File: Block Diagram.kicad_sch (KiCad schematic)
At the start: 0 parts

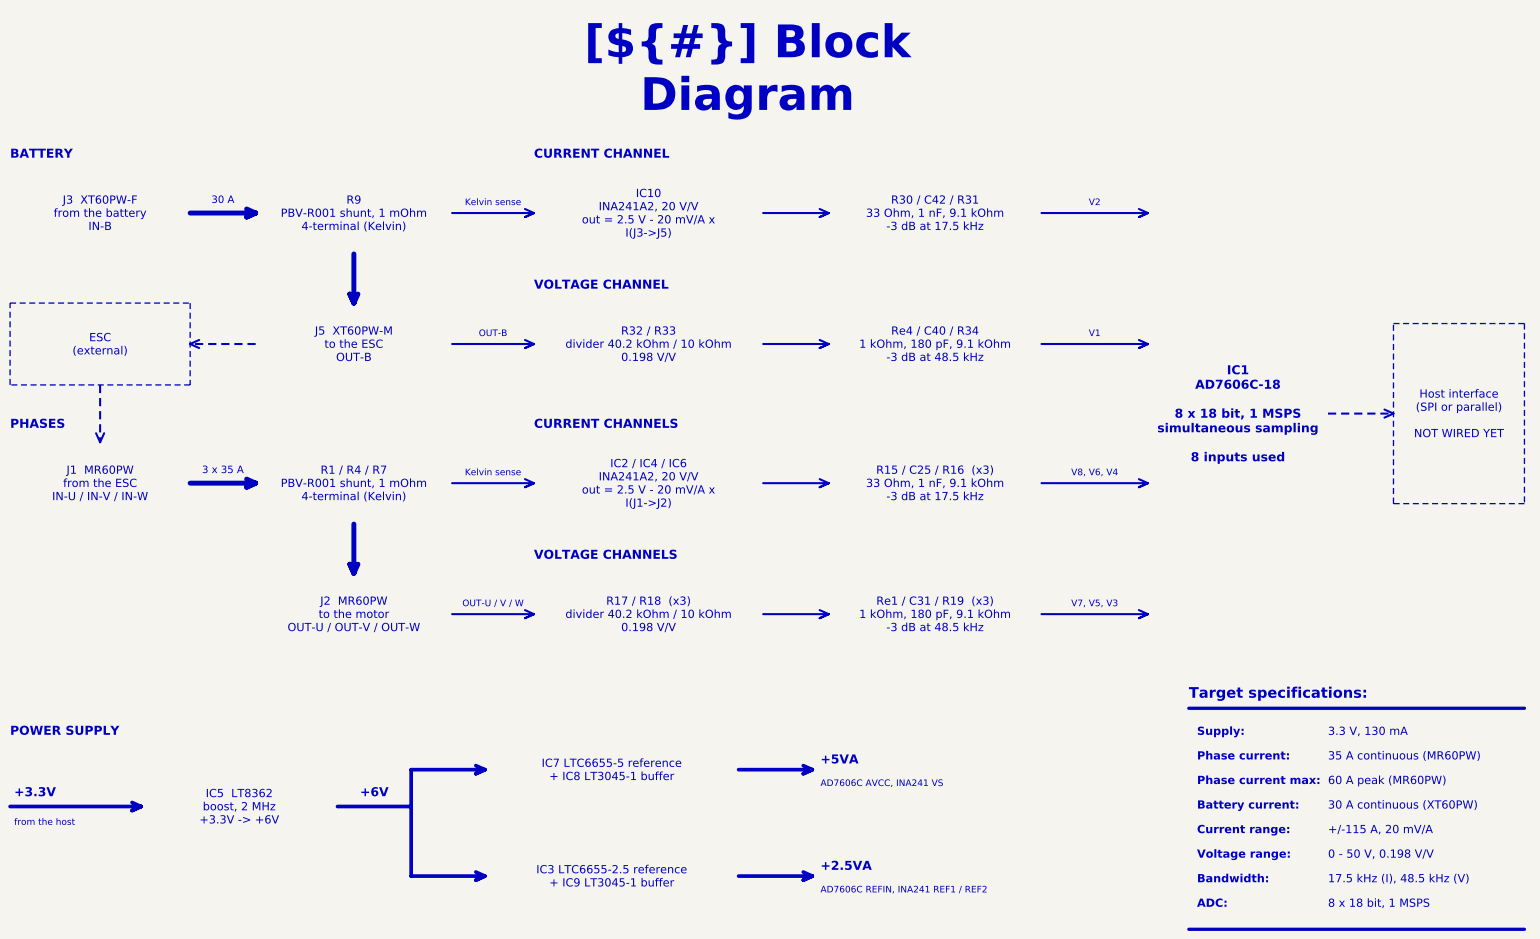
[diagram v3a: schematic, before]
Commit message: Restyle schematic sheets, new title block logo, WE-MAPI inductor in simulations
- Schematic sheets: restyled frames, tables and text boxes
- Title block: INGENIERIE FRANCE logo in KDT_Template_GIT.kicad_wks
- LTspice: L1 modelled as WE-MAPI 4030 74438357022 (22 mOhm),
  simulations 01 and 03 rerun, README and results updated

Co-Authored-By: Claude Opus 5.5 <noreply@anthropic.com>
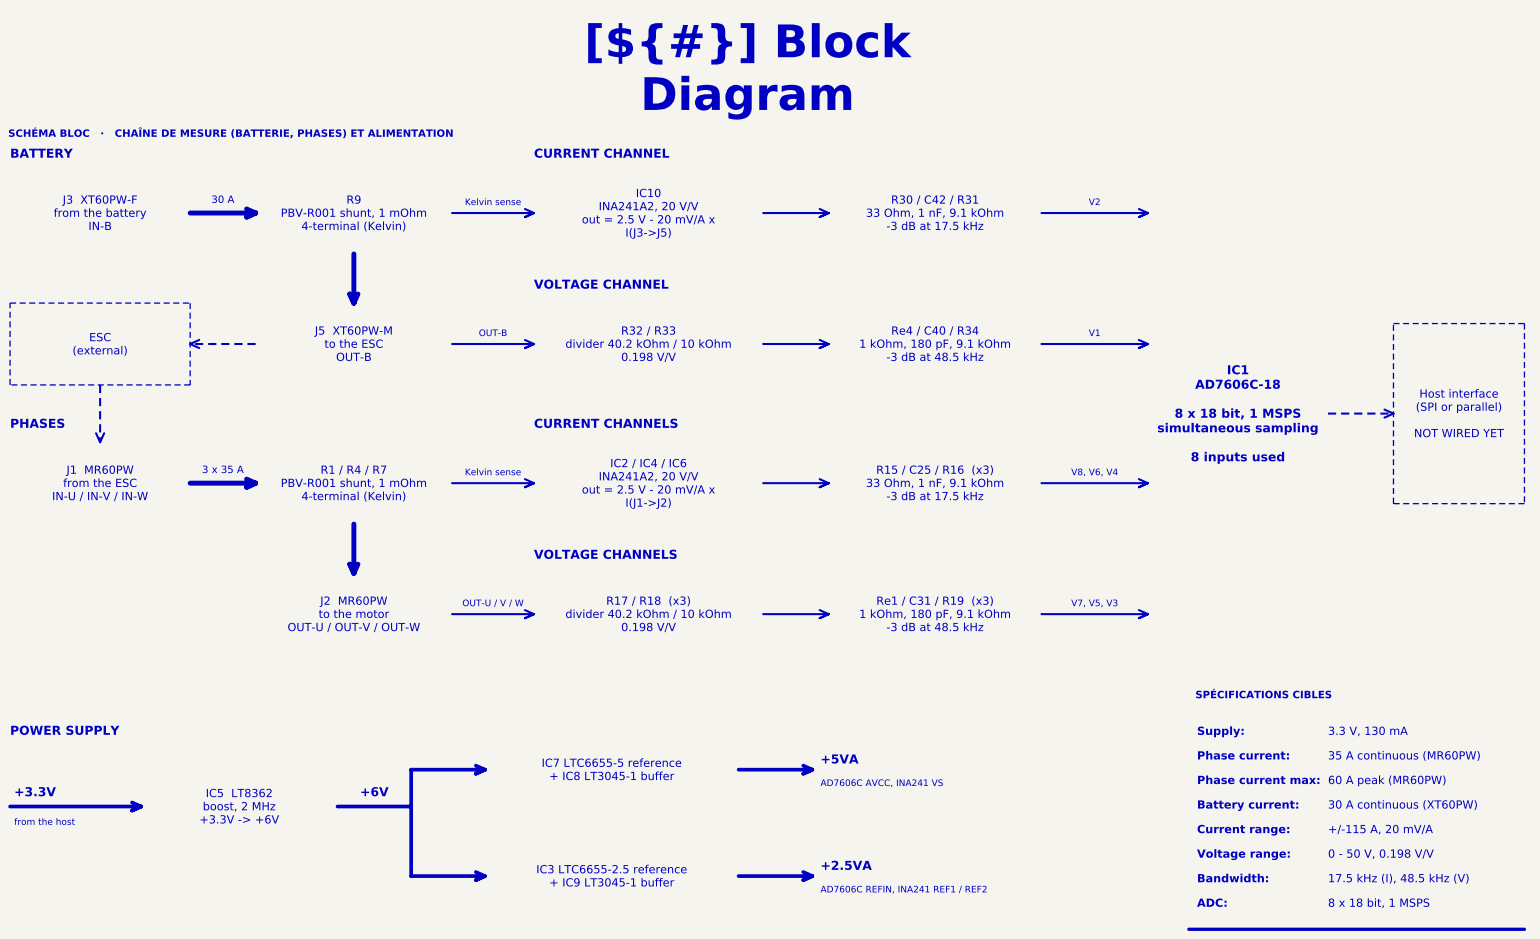
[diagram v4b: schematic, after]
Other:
- note removed: "Target specifications:"
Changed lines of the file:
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@@
-		)
-	)
-	(text "Target specifications:"
-		(exclude_from_sim no)
-		(at 318 181 0)
-		(effects
-			(font
-				(face "Arial")
-				(size 2.6 2.6)
-				(bold yes)
-				(color 0 0 0 1)
-			)
-			(justify left bottom)
 		)
 	)
@@
 	(polyline
 		(pts
-			(xy 318 183) (xy 400 183)
-		)
-		(stroke
-			(width 0.8)
-			(type default)
-			(color 0 0 0 1)
-		)
-	)
-	(polyline
-		(pts
 			(xy 110 207) (xy 128 207)
 		)
@@
 		)
 	)
+	(text_box "SCHÉMA BLOC   ·   CHAÎNE DE MESURE (BATTERIE, PHASES) ET ALIMENTATION"
+		(exclude_from_sim no)
+		(at 27.94 39.37 0)
+		(size 373.38 6.35)
+		(margins 1.6 1.6 1.6 1.6)
+		(stroke
+			(width -0.0001)
+			(type solid)
+		)
+		(fill
+			(type color)
+			(color 162 22 34 1)
+		)
+		(effects
+			(font
+				(face "Arial")
+				(size 1.8 1.8)
+				(thickness 0.36)
+				(bold yes)
+				(color 255 255 255 1)
+			)
+			(justify left)
+		)
+	)
+	(text_box "SPÉCIFICATIONS CIBLES"
+		(exclude_from_sim no)
+		(at 318 176.53 0)
+		(size 82 6.35)
+		(margins 1.6 1.6 1.6 1.6)
+		(stroke
+			(width -0.0001)
+			(type solid)
+		)
+		(fill
+			(type color)
+			(color 0 105 120 1)
+		)
+		(effects
+			(font
+				(face "Arial")
+				(size 1.8 1.8)
+				(thickness 0.36)
+				(bold yes)
+				(color 255 255 255 1)
+			)
+			(justify left)
+		)
+	)

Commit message: Wire the AD7606C-18 digital side to host header J4, add test points
- AD7606C-18: software mode (OS0-2 high), serial (PAR/SER SEL high),
  REF SELECT low; CONVST, BUSY, RESET, CS, SCLK, SDI, FRSTDATA and
  DOUTA-D to J4 (2x8 pin header 2.54 mm, horizontal), +3.3V on J4 pin 1
- AD7606C-18 AGND pin 26 and REFGND pin 46 on GND
- Test points TP1-TP16: rails, INA241 outputs, CONVST, BUSY
- Nets renamed SHUNT_*, INA_*, ADC_*; net colours in the project
- LT3045-1 footprint: thermal vias numbered as exposed pad 13
- PCB updated from the schematic; ADC_* digital nets not routed yet
- README template / CHANGELOG: status, J4 pinout, design review 1 and 2
  fixed, new finding 9 (VDRIVE above AVCC + 0.3 V at power-up),
  4 channels / 8 ADC inputs

Co-Authored-By: Claude Opus 5.5 <noreply@anthropic.com>
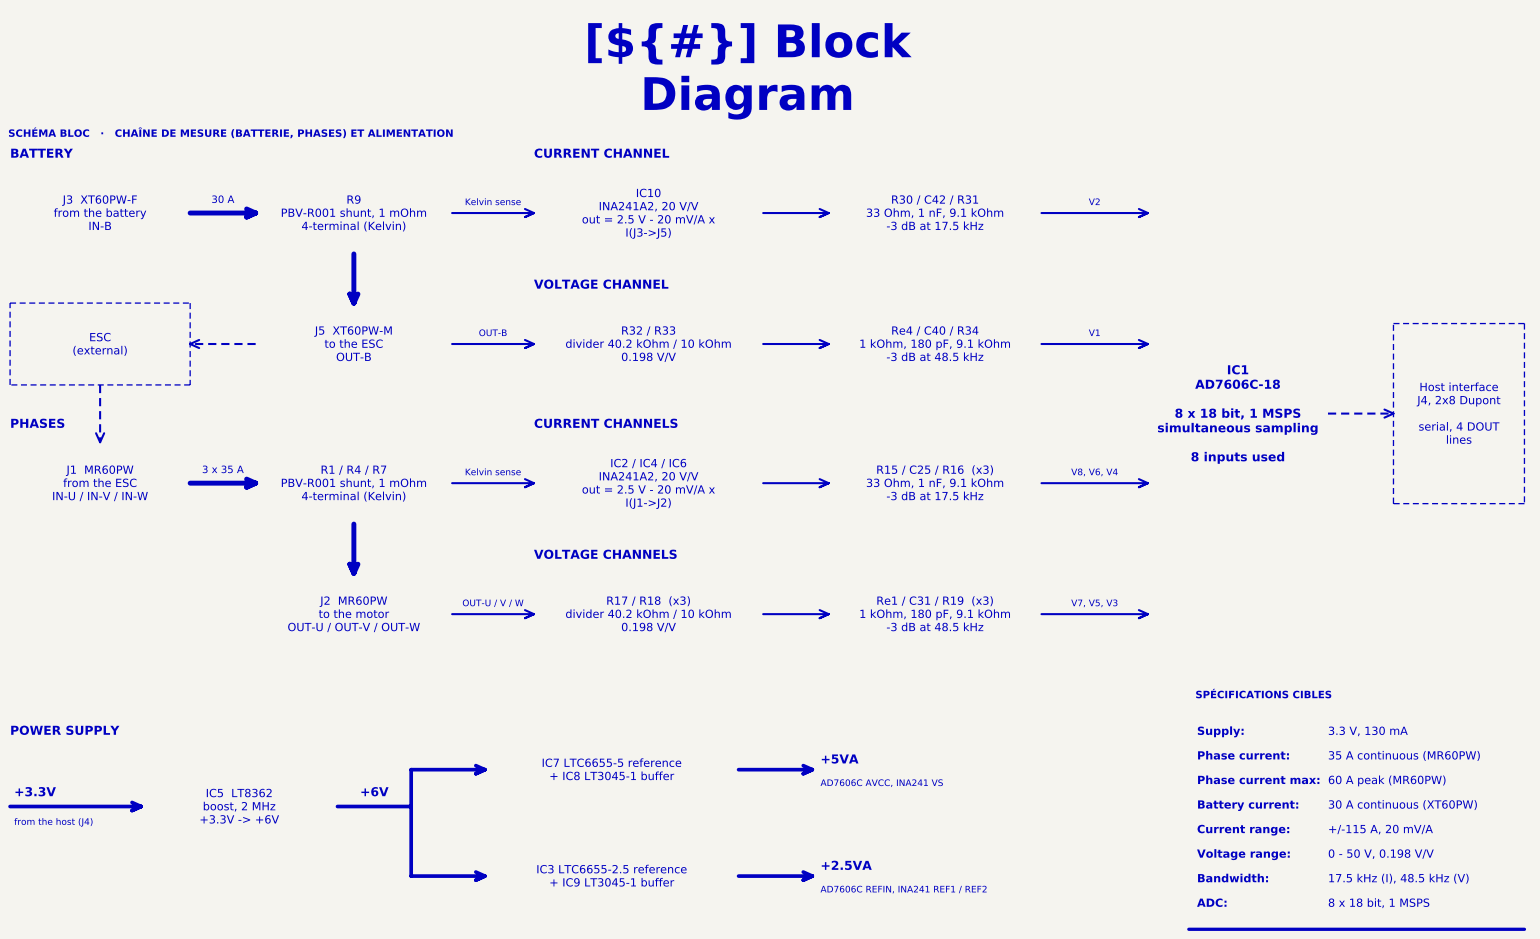
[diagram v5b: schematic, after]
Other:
- note added: "from the host (J4)"
- note removed: "from the host"
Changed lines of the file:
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@@
 		)
 	)
-	(text "from the host"
+	(text "from the host (J4)"
 		(exclude_from_sim no)
 		(at 31 211 0)
@@
 		)
 	)
-	(text_box "Host interface\n(SPI or parallel)\n\nNOT WIRED YET"
+	(text_box "Host interface\nJ4, 2x8 Dupont\n\nserial, 4 DOUT lines"
 		(exclude_from_sim no)
 		(at 368 89 0)
@@
 		)
 	)
+	(text_box "SCHÉMA BLOC   ·   CHAÎNE DE MESURE (BATTERIE, PHASES) ET ALIMENTATION"
+		(exclude_from_sim no)
+		(at 27.94 39.37 0)
+		(size 373.38 6.35)
+		(margins 1.6 1.6 1.6 1.6)
+		(stroke
+			(width -0.0001)
+			(type solid)
+		)
+		(fill
+			(type color)
+			(color 162 22 34 1)
+		)
+		(effects
+			(font
+				(face "Arial")
+				(size 1.8 1.8)
+				(thickness 0.36)
+				(bold yes)
+				(color 255 255 255 1)
+			)
+			(justify left)
+		)
+	)
 	(text_box "R30 / C42 / R31\n33 Ohm, 1 nF, 9.1 kOhm\n-3 dB at 17.5 kHz"
 		(exclude_from_sim no)
@@
 				(color 255 255 255 1)
 			)
+		)
+	)
+	(text_box "SPÉCIFICATIONS CIBLES"
+		(exclude_from_sim no)
+		(at 318 176.53 0)
+		(size 82 6.35)
+		(margins 1.6 1.6 1.6 1.6)
+		(stroke
+			(width -0.0001)
+			(type solid)
+		)
+		(fill
+			(type color)
+			(color 0 105 120 1)
+		)
+		(effects
+			(font
+				(face "Arial")
+				(size 1.8 1.8)
+				(thickness 0.36)
+				(bold yes)
+				(color 255 255 255 1)
+			)
+			(justify left)
 		)
 	)
@@
 		)
 	)
-	(text_box "SCHÉMA BLOC   ·   CHAÎNE DE MESURE (BATTERIE, PHASES) ET ALIMENTATION"
-		(exclude_from_sim no)
-		(at 27.94 39.37 0)
-		(size 373.38 6.35)
-		(margins 1.6 1.6 1.6 1.6)
-		(stroke
-			(width -0.0001)
-			(type solid)
-		)
-		(fill
-			(type color)
-			(color 162 22 34 1)
-		)
-		(effects
-			(font
-				(face "Arial")
-				(size 1.8 1.8)
-				(thickness 0.36)
-				(bold yes)
-				(color 255 255 255 1)
-			)
-			(justify left)
-		)
-	)
-	(text_box "SPÉCIFICATIONS CIBLES"
-		(exclude_from_sim no)
-		(at 318 176.53 0)
-		(size 82 6.35)
-		(margins 1.6 1.6 1.6 1.6)
-		(stroke
-			(width -0.0001)
-			(type solid)
-		)
-		(fill
-			(type color)
-			(color 0 105 120 1)
-		)
-		(effects
-			(font
-				(face "Arial")
-				(size 1.8 1.8)
-				(thickness 0.36)
-				(bold yes)
-				(color 255 255 255 1)
-			)
-			(justify left)
-		)
-	)
